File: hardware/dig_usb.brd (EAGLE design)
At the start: 146.1 x 102.6 mm, 147 parts, among them IC1 AT90USB1287-AU, IC202 DS1337S, IC203 MAX487CSA, IC204 74HC166D, IC301 LTV-356T, IC302 LTV-356T, IC303 LTV-356T, IC304 LTV-356T, IC305 LTV-356T, IC306 LTV-356T, IC307 LTV-356T, IC308 LTV-356T, K401 S202S02, K402 S202S02, K403 S202S02, K404 S202S02, K405 S202S02, K406 S202S02, K407 S202S02, K408 S202S02, Q201 32,768kHz, T301 BCR191, T302 BCR191, T303 BCR191, T304 BCR191, T305 BCR191, T306 BCR191, T307 BCR191, T308 BCR191, X101 RIA-73-02, X201 ISP, X202 RIA-73-02, X301 RIA-73-02, X302 RIA-73-02, X303 RIA-73-02, X304 RIA-73-02, X305 RIA-73-02, X401 RIA-73-02, X402 RIA-73-02, X403 RIA-73-02, X404 RIA-73-02, X405 RIA-73-02

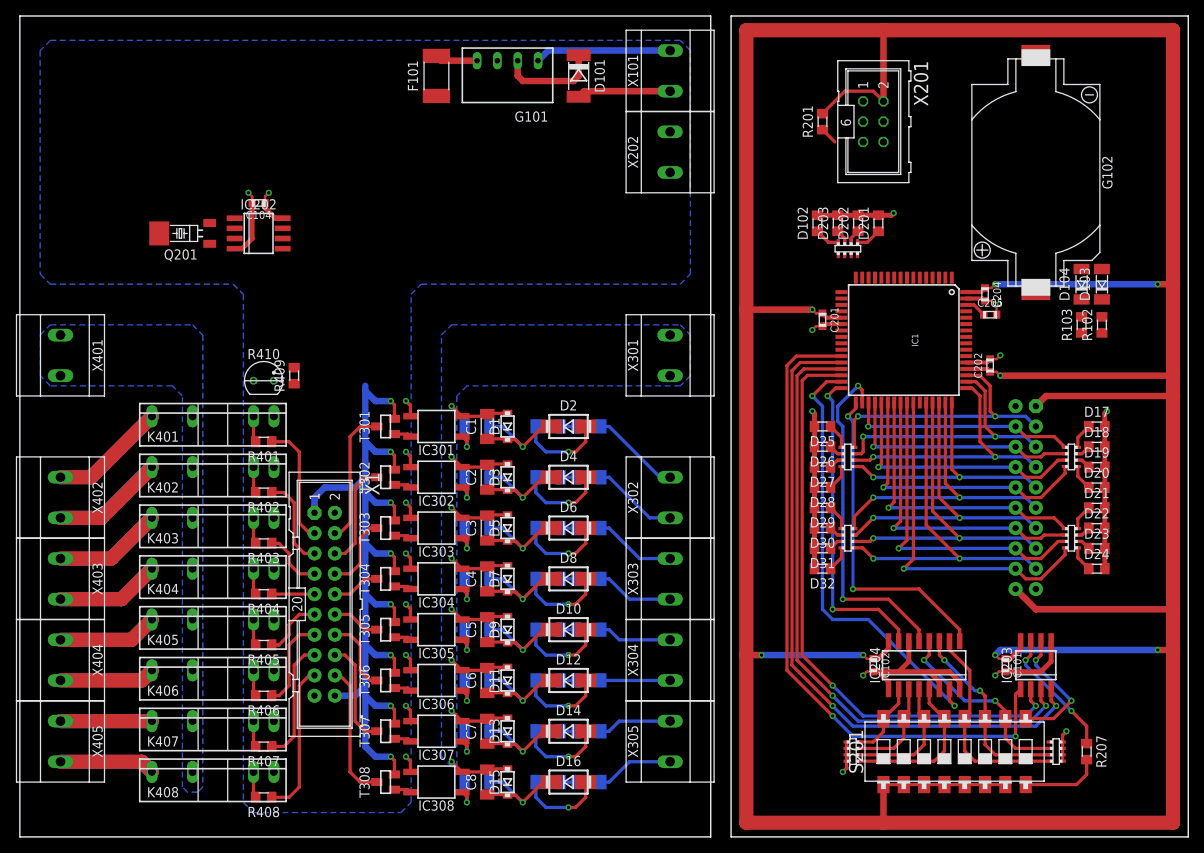
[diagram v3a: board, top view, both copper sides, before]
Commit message: USB Stecker und Quarz hinzugefügt
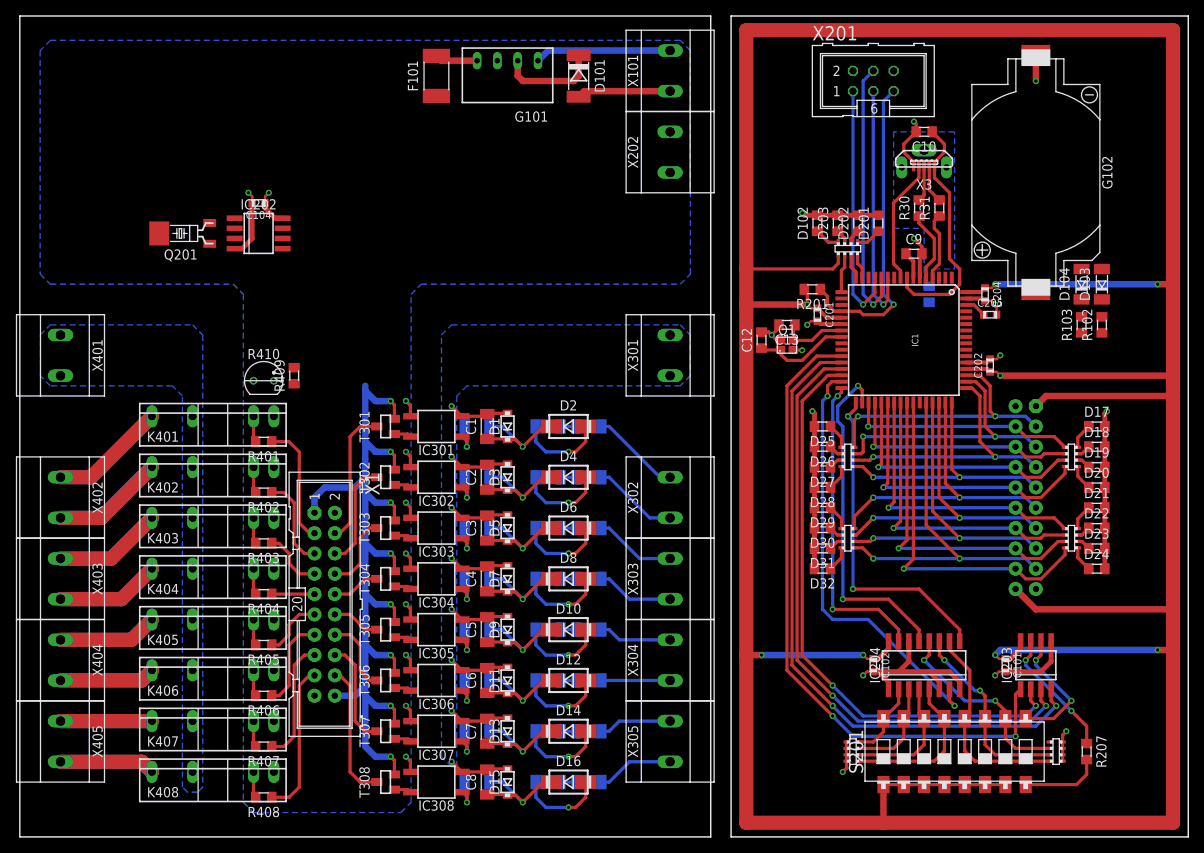
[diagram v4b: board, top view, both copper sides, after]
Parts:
- added C10: 10μF, passiv:CHIP_0805
- added C11: 100nF, passiv:CHIP_0805
- added C12, C13: 15pF, passiv:CHIP_0805
- added C9: 1μF, passiv:CHIP_0805
- added Q1: 16MHz, passiv:X22
- added R30, R31: 22Ω, passiv:CHIP_0805
- added X3: (no value), stecker:MOLEX_1051330011
- moved R201 21.0 mm to (99.1, 67.9), turned to 180 degrees
- moved X201 5.08 mm to (106.7, 94.0), turned to 0 degrees
- moved C201 0.90 mm to (99.7, 64.8)
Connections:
- removed net UGND: IC1.6
- removed net VBUS: IC1.8
- new net N$118: C9.1, IC1.7
- new net N$119: R30.2, X3.3
- new net N$120: IC1.5, R30.1
- new net N$121: R31.2, X3.2
- new net N$122: IC1.4, R31.1
- new net N$123: IC1.9, X3.4
- new net N$124: C10.1, IC1.8, X3.1
- new net N$125: C13.1, IC1.23, Q1.3
- new net N$128: C12.1, IC1.24, Q1.1
- new net USHIELD: C11.1, X3.S1, X3.S2, X3.S3
- net GND: now also C10.2, C11.2, C12.2, C13.2, C9.2, IC1.6, Q1.2, Q1.4, X3.5
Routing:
- net !RESET: track 2.18 -> 39.3 mm, vias 0 -> 1
- net MOSI: track 0.00 -> 34.0 mm, vias 0 -> 1
- net MISO: track 0.00 -> 31.2 mm, vias 0 -> 1
- net SCK: track 0.00 -> 30.8 mm, vias 0 -> 1
- net N$124: track 0.00 -> 30.2 mm
- net GND: track 130.4 -> 152.3 mm, vias 19 -> 24
- net N$123: track 0.00 -> 15.7 mm
- net N$128: track 0.00 -> 12.1 mm
- net N$120: track 0.00 -> 8.92 mm
- net N$122: track 0.00 -> 8.59 mm
- net N$125: track 0.00 -> 8.54 mm
- net N$121: track 0.00 -> 4.85 mm
- net LED3: track 0.00 -> 4.80 mm
- net N$119: track 0.00 -> 4.59 mm
- net N$118: track 0.00 -> 3.38 mm
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- added copper zone on layer 16, net USHIELD

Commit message: dig_usb vorläufig komplett geroutet
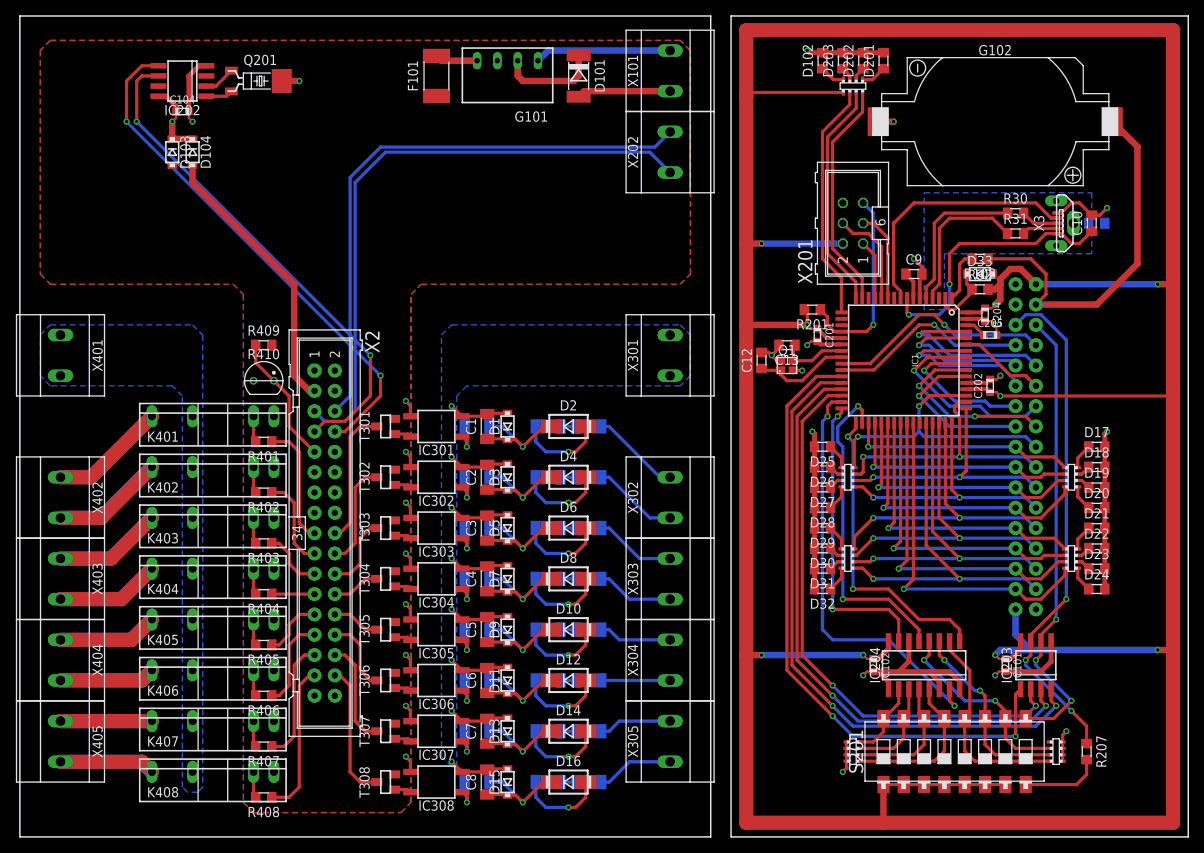
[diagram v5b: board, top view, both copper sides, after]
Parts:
- removed R103: 1MΩ, passiv:CHIP_0805
- removed X1: (no value), anschluss:WS20V
- added D33: MMSZ5222BT1, diode:SOD123
- added R32: 10kΩ, passiv:CHIP_0805
- added X4: (no value), anschluss:WS34V
- D103, D104: device diode:MINIMELF -> diode:SOD123
- X2: device anschluss:WS20V -> anschluss:WS34V
- moved D103 117.4 mm to (19.1, 85.1), turned to 270 degrees
- moved D104 112.3 mm to (21.6, 85.1), turned to 270 degrees
- moved X2 87.7 mm to (38.1, 37.5), flipped to the top
- moved C10 23.9 mm to (134.0, 76.2), turned to 90 degrees
- moved C11 22.8 mm to (134.6, 76.2), turned to 180 degrees
- moved IC202 21.3 mm to (20.3, 94.0), turned to 90 degrees
- moved D102 20.3 mm to (100.3, 96.5)
- moved D201 20.3 mm to (108.0, 96.5)
- moved D202 20.3 mm to (105.4, 96.5)
- moved D203 20.3 mm to (102.9, 96.5)
- moved R29 20.3 mm to (104.1, 93.3)
- moved Q201 19.9 mm to (27.9, 94.0), turned to 270 degrees
- moved X201 18.0 mm to (104.1, 76.2), turned to 90 degrees
- moved X3 17.9 mm to (129.5, 76.2), turned to 90 degrees
- moved R102 17.3 mm to (120.0, 71.8), turned to 180 degrees
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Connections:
- removed net ALARM1: IC1.18, IC202.3
- removed net ALARM2: IC1.19, IC202.7
- removed net BAT: IC1.55, R102.1, R103.2
- removed net SCL: IC1.25, IC202.6
- removed net SDA: IC1.26, IC202.5
- removed net TEMP: IC1.54, R409.1, R410.1
- new net N$129: D33.K, IC1.2, R32.1
- new net N$130: D104.A, X2.3
- new net N$131: IC202.6, X2.7
- new net N$132: IC202.5, X2.8
- new net N$133: X2.6, X202.2
- new net N$134: X2.5, X202.1
- new net N$135: IC1.61, X4.9
- new net N$136: IC1.60, X4.10
- new net N$137: IC1.59, X4.11
- new net N$138: IC1.58, X4.12
- new net N$139: IC1.57, X4.13
- new net N$140: IC1.56, X4.14
- new net N$141: IC1.55, X4.15
- new net N$142: IC1.54, X4.16
- new net N$143: G102.+, R102.1, X4.3
- new net N$144: IC1.25, X4.7
- new net N$145: IC1.26, X4.8
- new net N$146: R409.1, R410.1, X2.9
- net +5V: now also R32.2, X2.34, X4.1, X4.34; no longer X1.1, X1.20, X2.20
- net GND: now also D33.A, X2.33, X2.4, X4.2, X4.33, X4.4; no longer R103.1, X1.19, X1.2, X2.19
- net IN0: now also X4.18; no longer X2.4
- net IN1: now also X4.20; no longer X2.6
- net IN2: now also X4.22; no longer X2.8
- net IN3: now also X4.24; no longer X2.10
- net IN4: now also X4.26; no longer X2.12
- net IN5: now also X4.28; no longer X2.14
- net IN6: now also X4.30; no longer X2.16
- net IN7: now also X4.32; no longer X2.18
- net N$100: now also X2.30; no longer X1.16
- net N$101: now also X2.32; no longer X1.18
- net N$20: now also X4.5; no longer X202.1
- net N$21: now also IC1.1; no longer D104.A, G102.+
- net N$22: now also X4.6; no longer X202.2
- net N$67: now also X2.17; no longer X1.3
- net N$79: now also X2.19; no longer X1.5
- net N$87: now also X2.21; no longer X1.7
- net N$88: now also X2.23; no longer X1.9
- net N$90: now also X2.25; no longer X1.11
- net N$91: now also X2.27; no longer X1.13
- net N$92: now also X2.29; no longer X1.15
- net N$93: now also X2.31; no longer X1.17
- net N$94: now also X2.18; no longer X1.4
- net N$95: now also X2.20; no longer X1.6
- net N$96: now also X2.22; no longer X1.8
- net N$97: now also X2.24; no longer X1.10
- net N$98: now also X2.26; no longer X1.12
- net N$99: now also X2.28; no longer X1.14
- net OUT0: now also X4.17; no longer X2.3
- net OUT1: now also X4.19; no longer X2.5
- net OUT2: now also X4.21; no longer X2.7
- net OUT3: now also X4.23; no longer X2.9
- net OUT4: now also X4.25; no longer X2.11
- net OUT5: now also X4.27; no longer X2.13
- net OUT6: now also X4.29; no longer X2.15
- net OUT7: now also X4.31; no longer X2.17
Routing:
- net +5V: track 597.6 -> 474.8 mm, vias 16 -> 9
- net N$134: track 0.00 -> 76.7 mm
- net N$133: track 0.00 -> 72.4 mm
- net N$132: track 0.00 -> 64.9 mm, vias 0 -> 2
- net N$131: track 0.00 -> 63.3 mm, vias 0 -> 2
- net N$22: track 16.2 -> 63.9 mm, vias 2 -> 3
- net N$143: track 0.00 -> 46.3 mm
- net N$20: track 16.2 -> 57.6 mm, vias 2 -> 3
- net N$130: track 0.00 -> 34.9 mm
- net N$144: track 0.00 -> 28.4 mm, vias 0 -> 1
- net LED1: track 3.07 -> 28.8 mm
- net LED2: track 3.07 -> 28.6 mm
- net N$139: track 0.00 -> 25.4 mm, vias 0 -> 1
- net N$145: track 0.00 -> 25.2 mm, vias 0 -> 1
- net LED3: track 4.80 -> 29.9 mm
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- added copper zone on layer 1, net +5V
